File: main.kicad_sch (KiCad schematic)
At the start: 2 parts

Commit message: Adding control stuff
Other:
- sheet boost_control_a renamed boost_a_control
- sheet boost_control_b renamed boost_b_control
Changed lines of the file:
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@@
 			(color 0 0 0 0.0000)
 		)
-		(property "Sheetname" "boost_control_a"
+		(property "Sheetname" "boost_a_control"
 			(at 119.38 125.0184 0)
 			(effects
@@
 	)
 	(sheet
-		(at 58.42 196.85)
+		(at 58.42 203.2)
 		(size 29.21 15.24)
 		(exclude_from_sim no)
@@
 		)
 		(property "Sheetname" "housekeeping"
-			(at 58.42 196.1384 0)
+			(at 58.42 202.4884 0)
 			(effects
 				(font
@@
 		)
 		(property "Sheetfile" "housekeeping.kicad_sch"
-			(at 58.42 212.6746 0)
+			(at 58.42 219.0246 0)
 			(effects
 				(font
@@
 			(color 0 0 0 0.0000)
 		)
-		(property "Sheetname" "boost_control_b"
+		(property "Sheetname" "boost_b_control"
 			(at 119.38 147.8784 0)
 			(effects

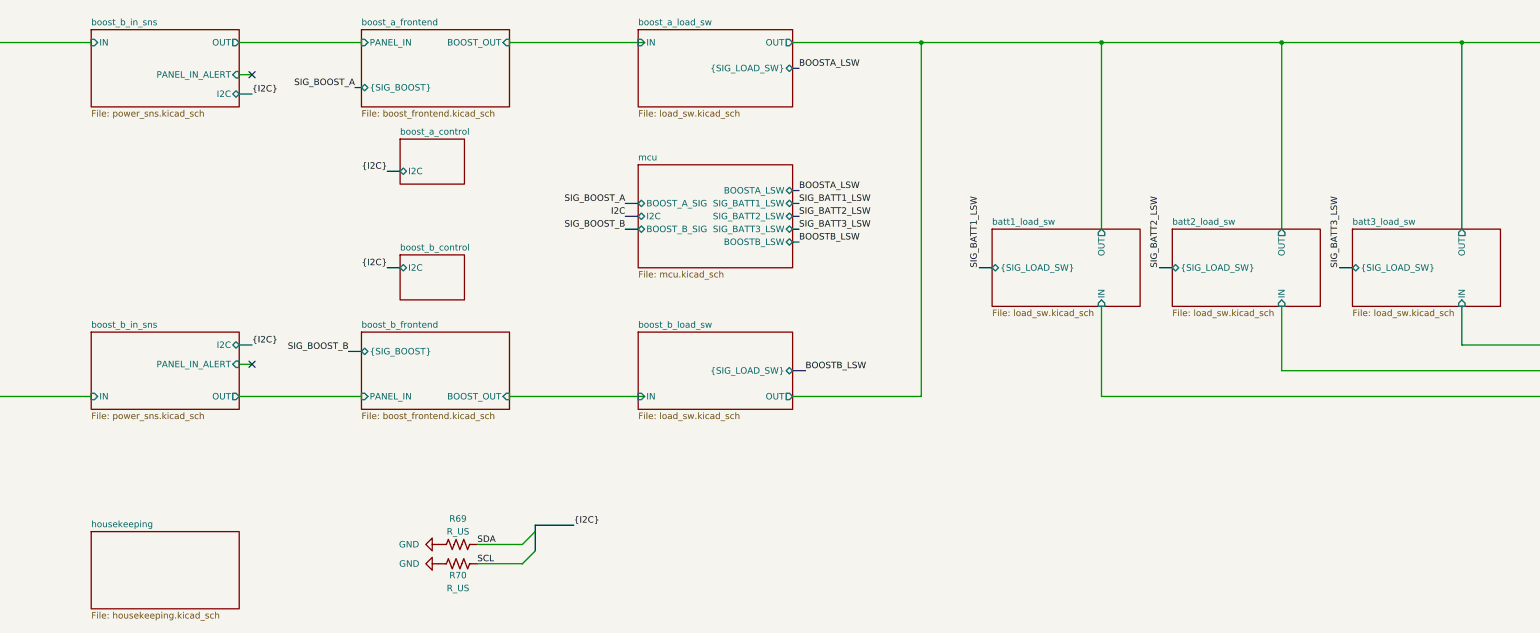
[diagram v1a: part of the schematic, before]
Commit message: Adding in connections to schematic
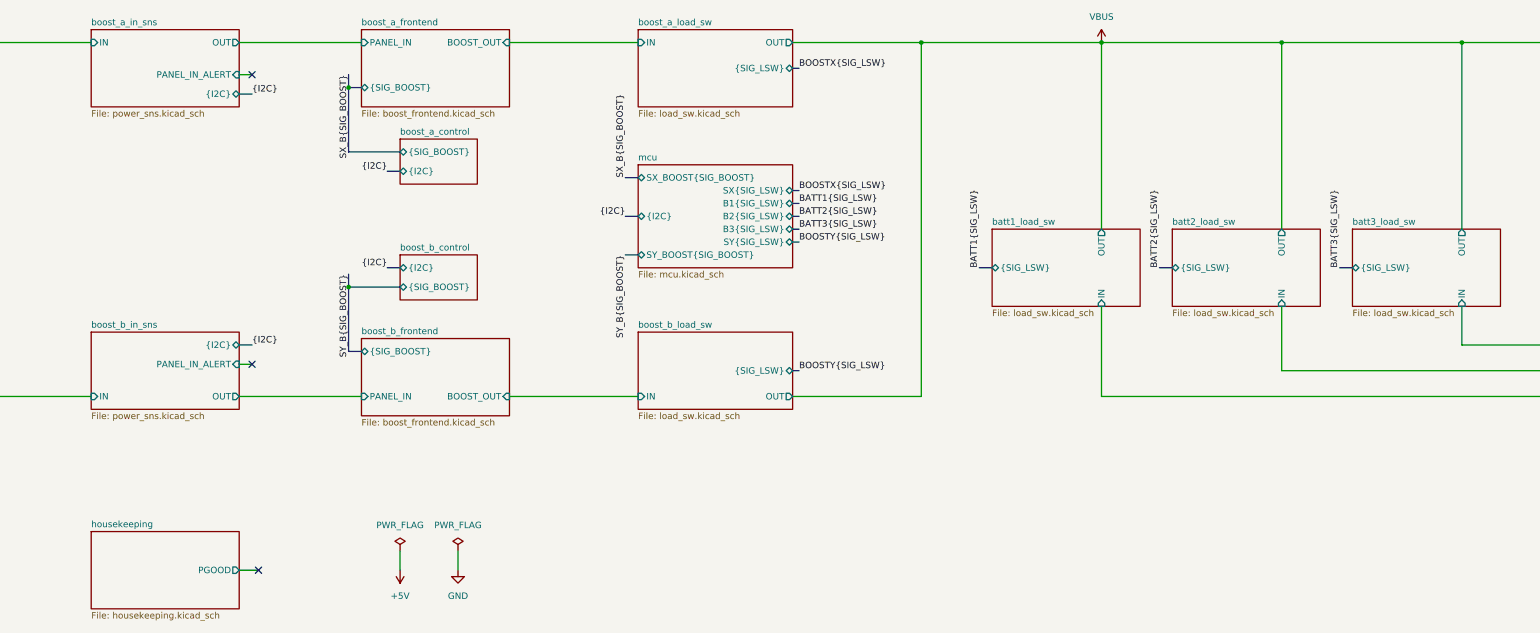
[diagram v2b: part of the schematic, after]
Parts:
- removed R69, R70: R_US, symbol Device:R_US
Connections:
- no-connect marks 2 -> 3
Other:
- added sheet boost_a_in_sns (power_sns.kicad_sch)
- sheet batt1_load_sw ports: added {SIG_LSW}; removed {SIG_LOAD_SW}
- sheet batt2_load_sw ports: added {SIG_LSW}; removed {SIG_LOAD_SW}
- sheet batt3_load_sw ports: added {SIG_LSW}; removed {SIG_LOAD_SW}
- sheet boost_a_control ports: added {I2C}, {SIG_BOOST}; removed I2C
- sheet boost_a_load_sw ports: added {SIG_LSW}; removed {SIG_LOAD_SW}
- sheet boost_b_control ports: added {I2C}, {SIG_BOOST}; removed I2C
- sheet boost_b_in_sns ports: added {I2C}; removed I2C
- sheet boost_b_load_sw ports: added {SIG_LSW}; removed {SIG_LOAD_SW}
- sheet housekeeping ports: added PGOOD; removed none
- sheet mcu ports: added B1{SIG_LSW}, B2{SIG_LSW}, B3{SIG_LSW}, SX_BOOST{SIG_BOOST}, SX{SIG_LSW}, SY_BOOST{SIG_BOOST}, SY{SIG_LSW}, {I2C}; removed BOOSTA_LSW, BOOSTB_LSW, BOOST_A_SIG, BOOST_B_SIG, I2C, SIG_BATT1_LSW, SIG_BATT2_LSW, SIG_BATT3_LSW
- company: (none) -> Solar Airplane
- title: (none) -> Power Board

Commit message: Working on layout now
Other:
- sheet connectors ports: added BATT3_DRV; removed BACKUP_BATT_DRV
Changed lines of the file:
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@@
 		(dnp no)
 		(fields_autoplaced yes)
-		(property "Reference" "#FLG014"
+		(property "Reference" "#FLG02"
 			(at 130.81 205.105 0)
 			(effects
@@
 			(project "PowerBoard"
 				(path "/99785679-20de-4827-b4cc-bc3c187068c9/9564929a-642e-4163-88c2-45054b63a5ed"
-					(reference "#FLG014")
+					(reference "#FLG02")
 					(unit 1)
 				)
@@
 		(dnp no)
 		(fields_autoplaced yes)
-		(property "Reference" "#PWR0133"
+		(property "Reference" "#PWR03"
 			(at 257.81 110.49 0)
 			(effects
@@
 			(project ""
 				(path "/99785679-20de-4827-b4cc-bc3c187068c9/9564929a-642e-4163-88c2-45054b63a5ed"
-					(reference "#PWR0133")
+					(reference "#PWR03")
 					(unit 1)
 				)
@@
 		(dnp no)
 		(fields_autoplaced yes)
-		(property "Reference" "#PWR0135"
+		(property "Reference" "#PWR02"
 			(at 130.81 217.17 0)
 			(effects
@@
 			(project ""
 				(path "/99785679-20de-4827-b4cc-bc3c187068c9/9564929a-642e-4163-88c2-45054b63a5ed"
-					(reference "#PWR0135")
+					(reference "#PWR02")
 					(unit 1)
 				)
@@
 		(dnp no)
 		(fields_autoplaced yes)
-		(property "Reference" "#FLG013"
+		(property "Reference" "#FLG01"
 			(at 119.38 205.105 0)
 			(effects
@@
 			(project ""
 				(path "/99785679-20de-4827-b4cc-bc3c187068c9/9564929a-642e-4163-88c2-45054b63a5ed"
-					(reference "#FLG013")
+					(reference "#FLG01")
 					(unit 1)
 				)
@@
 		(dnp no)
 		(fields_autoplaced yes)
-		(property "Reference" "#PWR0115"
+		(property "Reference" "#PWR01"
 			(at 119.38 207.01 0)
 			(effects
@@
 			(project ""
 				(path "/99785679-20de-4827-b4cc-bc3c187068c9/9564929a-642e-4163-88c2-45054b63a5ed"
-					(reference "#PWR0115")
+					(reference "#PWR01")
 					(unit 1)
 				)
@@
 			)
 		)
-		(pin "BACKUP_BATT_DRV" output
+		(pin "BATT3_DRV" output
 			(at 381 166.37 180)
 			(effects

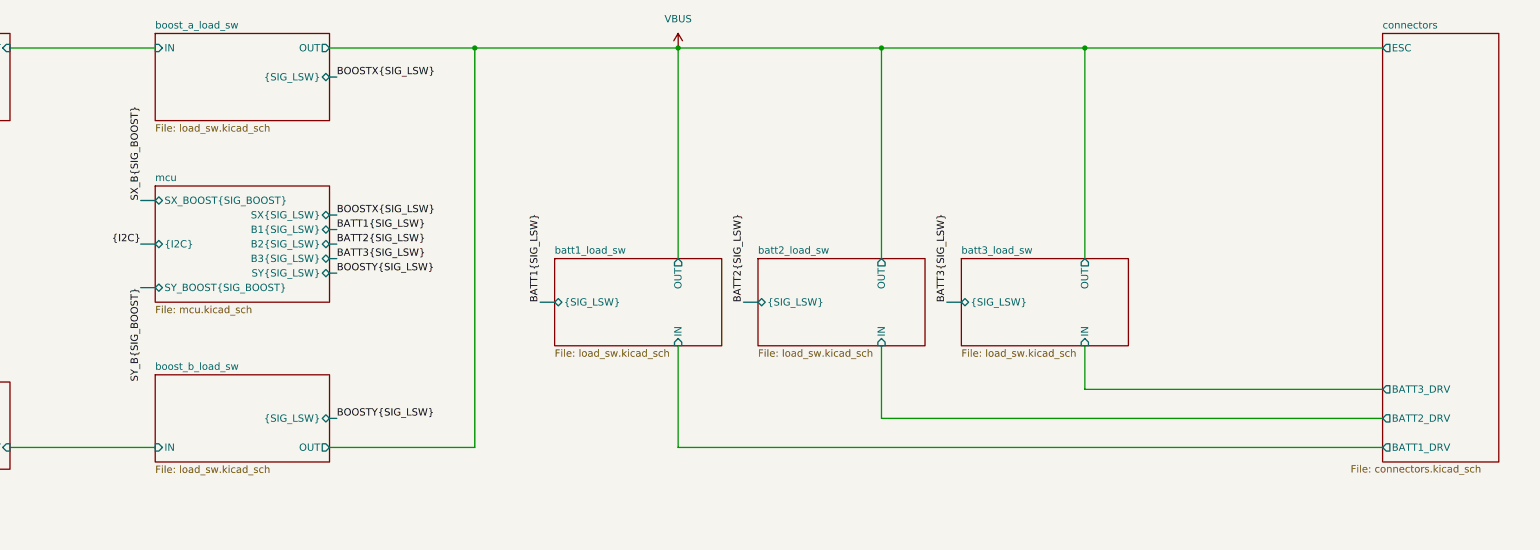
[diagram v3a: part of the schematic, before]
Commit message: imu and load switch for navlight
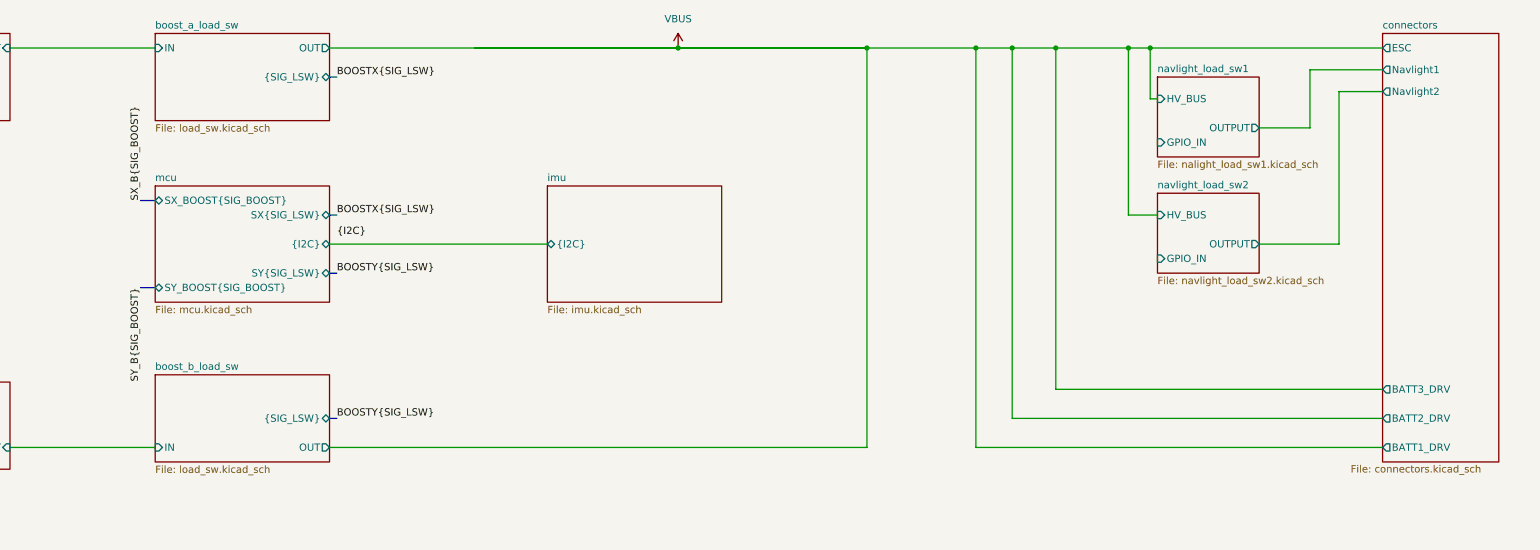
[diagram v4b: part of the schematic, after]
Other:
- removed sheet batt1_load_sw
- removed sheet batt2_load_sw
- removed sheet batt3_load_sw
- added sheet imu (imu.kicad_sch)
- added sheet navlight_load_sw1 (nalight_load_sw1.kicad_sch)
- added sheet navlight_load_sw2 (navlight_load_sw2.kicad_sch)
- sheet connectors ports: added Navlight1, Navlight2; removed none
- sheet mcu ports: added none; removed B1{SIG_LSW}, B2{SIG_LSW}, B3{SIG_LSW}

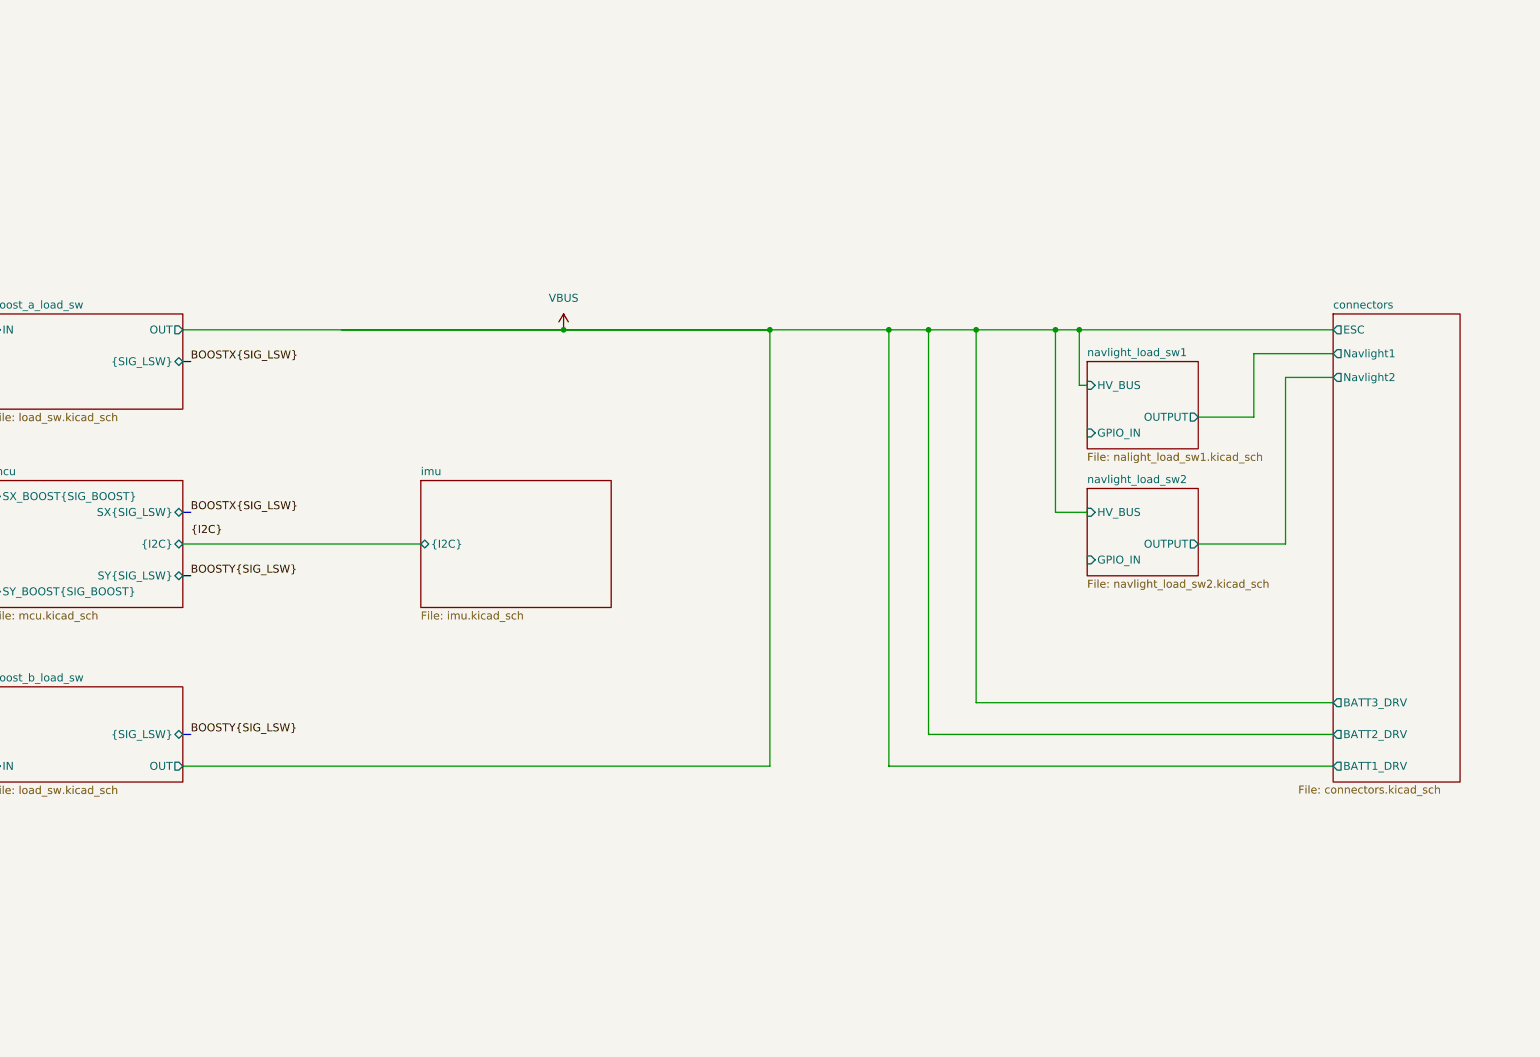
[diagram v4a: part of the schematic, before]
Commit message: PowerBoard update with LVBUS
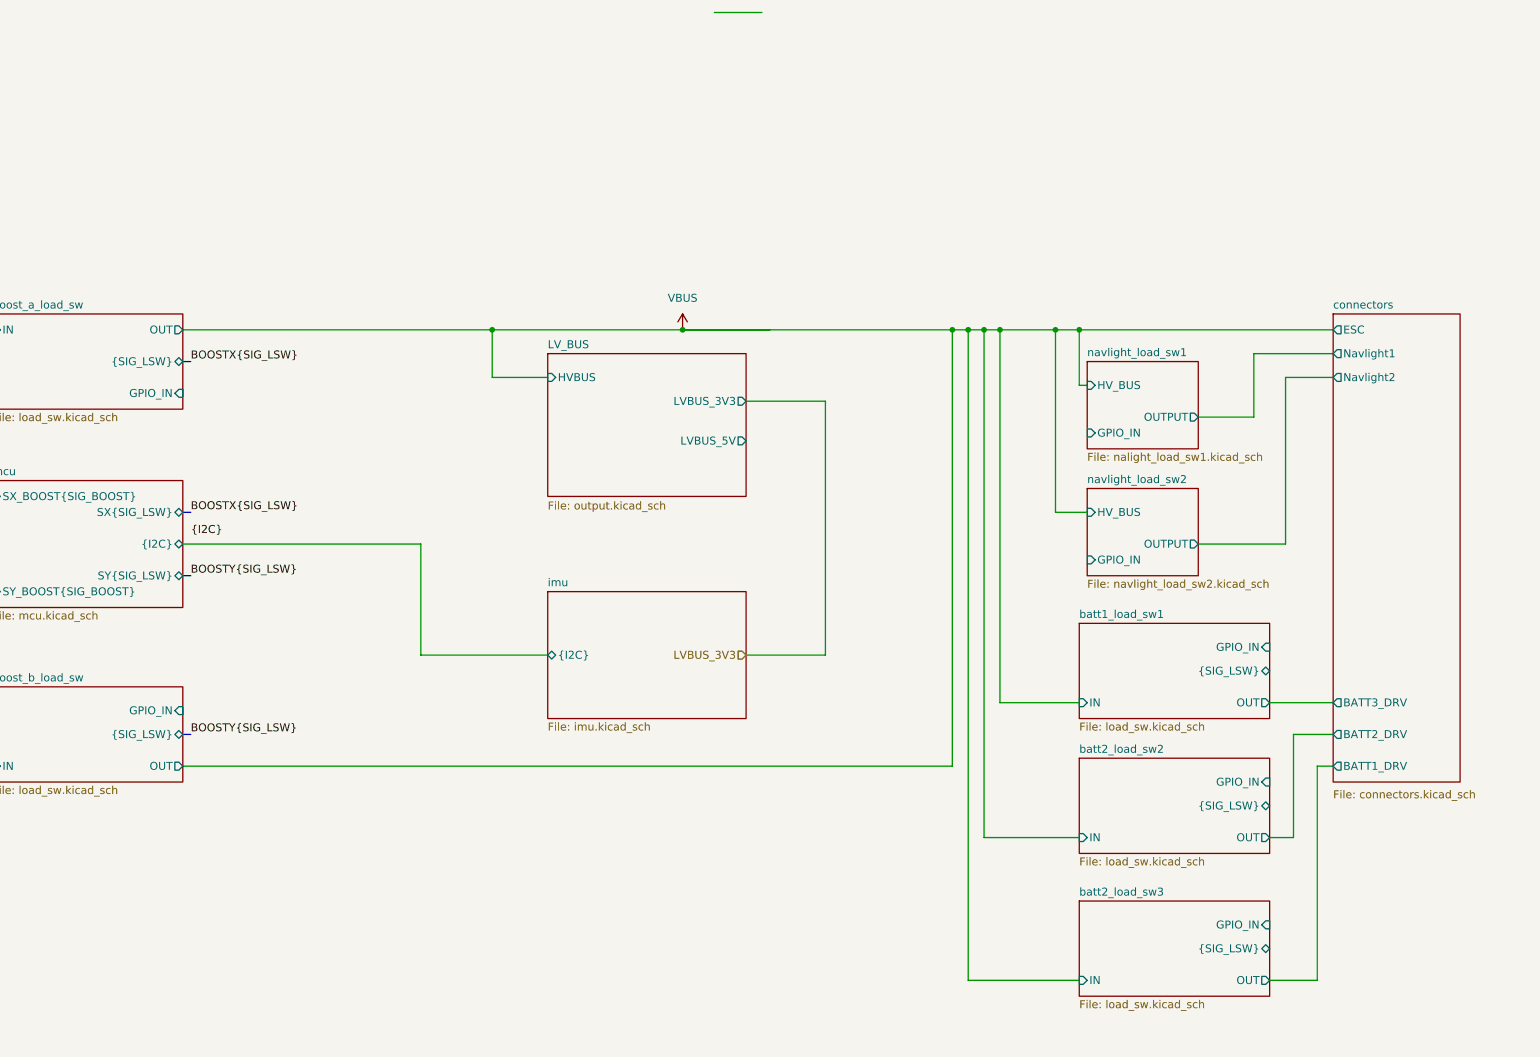
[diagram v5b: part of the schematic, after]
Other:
- added sheet LV_BUS (output.kicad_sch)
- added sheet batt1_load_sw1 (load_sw.kicad_sch)
- added sheet batt2_load_sw2 (load_sw.kicad_sch)
- added sheet batt2_load_sw3 (load_sw.kicad_sch)
- sheet boost_a_load_sw ports: added GPIO_IN; removed none
- sheet boost_b_load_sw ports: added GPIO_IN; removed none

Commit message: Cleaning up schematic
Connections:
- no-connect marks 3 -> 1
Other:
- sheet batt1_load_sw1 renamed batt1_lsw
- sheet batt2_load_sw2 renamed batt2_lsw
- removed sheet batt2_load_sw3
- removed sheet boost_a_load_sw
- removed sheet boost_b_load_sw
- removed sheet housekeeping
- added sheet boost_a_diode (ideal_diode.kicad_sch)
- added sheet boost_b_diode (ideal_diode.kicad_sch)
- sheet LV_BUS ports: added none; removed LVBUS_3V3, LVBUS_5V
- sheet batt1_lsw ports: added none; removed GPIO_IN
- sheet batt2_lsw ports: added none; removed GPIO_IN
- sheet connectors ports: added none; removed BATT1_DRV
- sheet navlight_load_sw1: file nalight_load_sw1.kicad_sch -> navlight_lsw.kicad_sch
- sheet navlight_load_sw1 ports: added nFLT; removed none
- sheet navlight_load_sw2: file navlight_load_sw2.kicad_sch -> navlight_lsw.kicad_sch
- sheet navlight_load_sw2 ports: added nFLT; removed none

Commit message: Working on it
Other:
- sheet LV_BUS ports: added HV_BUS; removed HVBUS
- sheet connectors ports: added BATT1_DRV, NAV1, NAV2; removed BATT3_DRV, Navlight1, Navlight2
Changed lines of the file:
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@@
+	)
+	(junction
+		(at 207.01 106.68)
+		(diameter 0)
+		(color 0 0 0 0)
 	)
 	(junction
@@
 	(wire
 		(pts
-			(xy 140.97 106.68) (xy 248.92 106.68)
+			(xy 140.97 106.68) (xy 207.01 106.68)
 		)
 		(stroke
@@
 	(wire
 		(pts
+			(xy 207.01 106.68) (xy 248.92 106.68)
+		)
+		(stroke
+			(width 0)
+			(type default)
+		)
+	)
+	(wire
+		(pts
 			(xy 248.92 106.68) (xy 289.56 106.68)
 		)
@@
 		)
 	)
+	(wire
+		(pts
+			(xy 207.01 106.68) (xy 207.01 177.8)
+		)
+		(stroke
+			(width 0)
+			(type default)
+		)
+	)
 	(bus
 		(pts
@@
 			(type default)
 			(color 0 194 0 1)
+		)
+	)
+	(wire
+		(pts
+			(xy 193.04 177.8) (xy 207.01 177.8)
+		)
+		(stroke
+			(width 0)
+			(type default)
 		)
 	)
@@
 			)
 		)
-		(pin "HVBUS" input
+		(pin "HV_BUS" input
 			(at 193.04 177.8 0)
 			(effects
@@
 			)
 		)
-		(pin "BATT3_DRV" output
-			(at 370.84 186.69 180)
-			(effects
-				(font
-					(size 1.27 1.27)
-				)
-				(justify left)
-			)
-		)
 		(pin "BATT2_DRV" output
 			(at 370.84 213.36 180)
@@
 			)
 		)
-		(pin "Navlight1" output
+		(pin "BATT1_DRV" input
+			(at 370.84 186.69 180)
+			(effects
+				(font
+					(size 1.27 1.27)
+				)
+				(justify left)
+			)
+		)
+		(pin "NAV1" output
 			(at 370.84 124.46 180)
 			(effects
@@
 			)
 		)
-		(pin "Navlight2" output
+		(pin "NAV2" output
 			(at 370.84 151.13 180)
 			(effects
@@
 		)
 		(pin "OUT" output
+			(at 309.88 186.69 180)
+			(effects
+				(font
+					(size 1.27 1.27)
+				)
+				(justify left)
+			)
+		)
+		(pin "IN" input
 			(at 340.36 186.69 0)
 			(effects
@@
 				)
 				(justify right)
-			)
-		)
-		(pin "IN" input
-			(at 309.88 186.69 180)
-			(effects
-				(font
-					(size 1.27 1.27)
-				)
-				(justify left)
 			)
 		)
@@
 		)
 		(pin "OUT" output
+			(at 309.88 213.36 180)
+			(effects
+				(font
+					(size 1.27 1.27)
+				)
+				(justify left)
+			)
+		)
+		(pin "IN" input
 			(at 340.36 213.36 0)
 			(effects
@@
 			)
 		)
-		(pin "IN" input
-			(at 309.88 213.36 180)
-			(effects
-				(font
-					(size 1.27 1.27)
-				)
-				(justify left)
-			)
-		)
